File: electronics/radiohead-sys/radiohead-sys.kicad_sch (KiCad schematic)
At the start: 0 parts

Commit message: cleaning up radiohead system overview to blank slate
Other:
- note removed: "Device Table"
- note removed: "Radiohead Robot"
- title: RADIOHEAD -> Radio-Head Robot

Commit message: completing all major schematics, just need to add usb devices
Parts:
- added D1: LED_Small, symbol Device:LED_Small
- added J2: JETSON_NANO.J41, symbol Connector_Generic:Conn_02x20_Odd_Even
- added J3: JETSON_NANO.J50, symbol Connector_Generic:Conn_01x12
- added Q2: Q_PNP, symbol Device:Q_PNP
- added R1: R_Small, symbol Device:R_Small
- added SW1, SW2: SW_Push, symbol Switch:SW_Push
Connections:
- new net: D1.1 (K), R1.1
- new net: D1.2 (A), Q2.C
- new net: J3.11 (Pin_11), SW1.2
- new net: J3.12 (Pin_12), SW1.1
- new net: J3.5 (Pin_5), J3.6 (Pin_6)
- new net: J3.7 (Pin_7), SW2.2
- new net: J3.8 (Pin_8), SW2.1
- new net ARDUINO_COMM.J41.SPI1.CIPO: J2.21 (Pin_21)
- new net ARDUINO_COMM.J41.SPI1.COPI: J2.19 (Pin_19)
- new net ARDUINO_COMM.J41.SPI1.SCK: J2.23 (Pin_23)
- new net GND: R1.2
- new net SPEAKER.J41.I2S4.LRCK: J2.35 (Pin_35)
- new net SPEAKER.J41.I2S4.SCLK: J2.12 (Pin_12)
- new net SPEAKER.J41.I2S4.SDIN: J2.38 (Pin_38)
- new net SPEAKER.J41.I2S4.SDOUT: J2.40 (Pin_40)
- new net STATUS_LED0.J41.GPIO.OUT: J2.3 (Pin_3)
- new net STATUS_LEDX.<J41, ARDUINO_PINOUT>.GPIO.OUT: Q2.B
- new net VDD: Q2.E
- no-connect marks 0 -> 7
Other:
- added sheet arduino (arduino.kicad_sch)
- added sheet audio (audio.kicad_sch)
- note added: "Circuits to Build * Jetson Nano (wip) - Power, reset buttons (done) - Camera (wip) - Screen(done) - Audio (done) - Microphone (wip) - Status lights (LEDs) (done) - Internet (done) * Arduino/Jetson Interface (done) * Arduino (wip) - pot/knob controller (done) - Servo limit switch (done) - Servo Driver (done) - Status Lights (done) * Power System (todo)"
- note added: "Developer Kit Module Interfaces"
- note added: "J41.P24.SPI1.CS0"
- note added: "Jetson Nano Wiring"
- note added: "Microphone Investigation Curretnly, we have the OSEPP Sound Sensor Module, that gives us an analog voltage reading of the current environmental noise. We would need to pass these values back which would be a bit of a pain. Or if we want the jetson nano to analyze them. Note also the OSEPP sound sensor is made for sound ranges 10-55Hz, whereas human noise is in the ~90-155Hz for male. I think the 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"
- note added: "P.5 + P.6, disable auto-on P.7 + P.8, switch for reset P.11 + P.12, switch for power-on"
- note added: "SPI Alt COPI -> MOSI CIPO -> MISO"
- note added: "SPI Resources - https://learn.sparkfun.com/tutorials/serial-peripheral-interface-spi/all Audio Resources - https://www.sparkfun.com/sparkfun-i2s-audio-breakout-max98357a.html Screen Resources - https://www.adafruit.com/product/1680 - https://www.adafruit.com/product/2218 Camera Resources - https://marketplace.nvidia.com/en-us/enterprise/robotics-edge/?category=cameras&page=1&limit=15 - https://de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"
- note added: "Status LEDs schematic for Jetson Nano and Arduino"
- note added: "Sub-Circuits"
- note added: "To Do List"
- note added: "x2"
- title: Radio-Head Robot -> Radiohead Animatronic

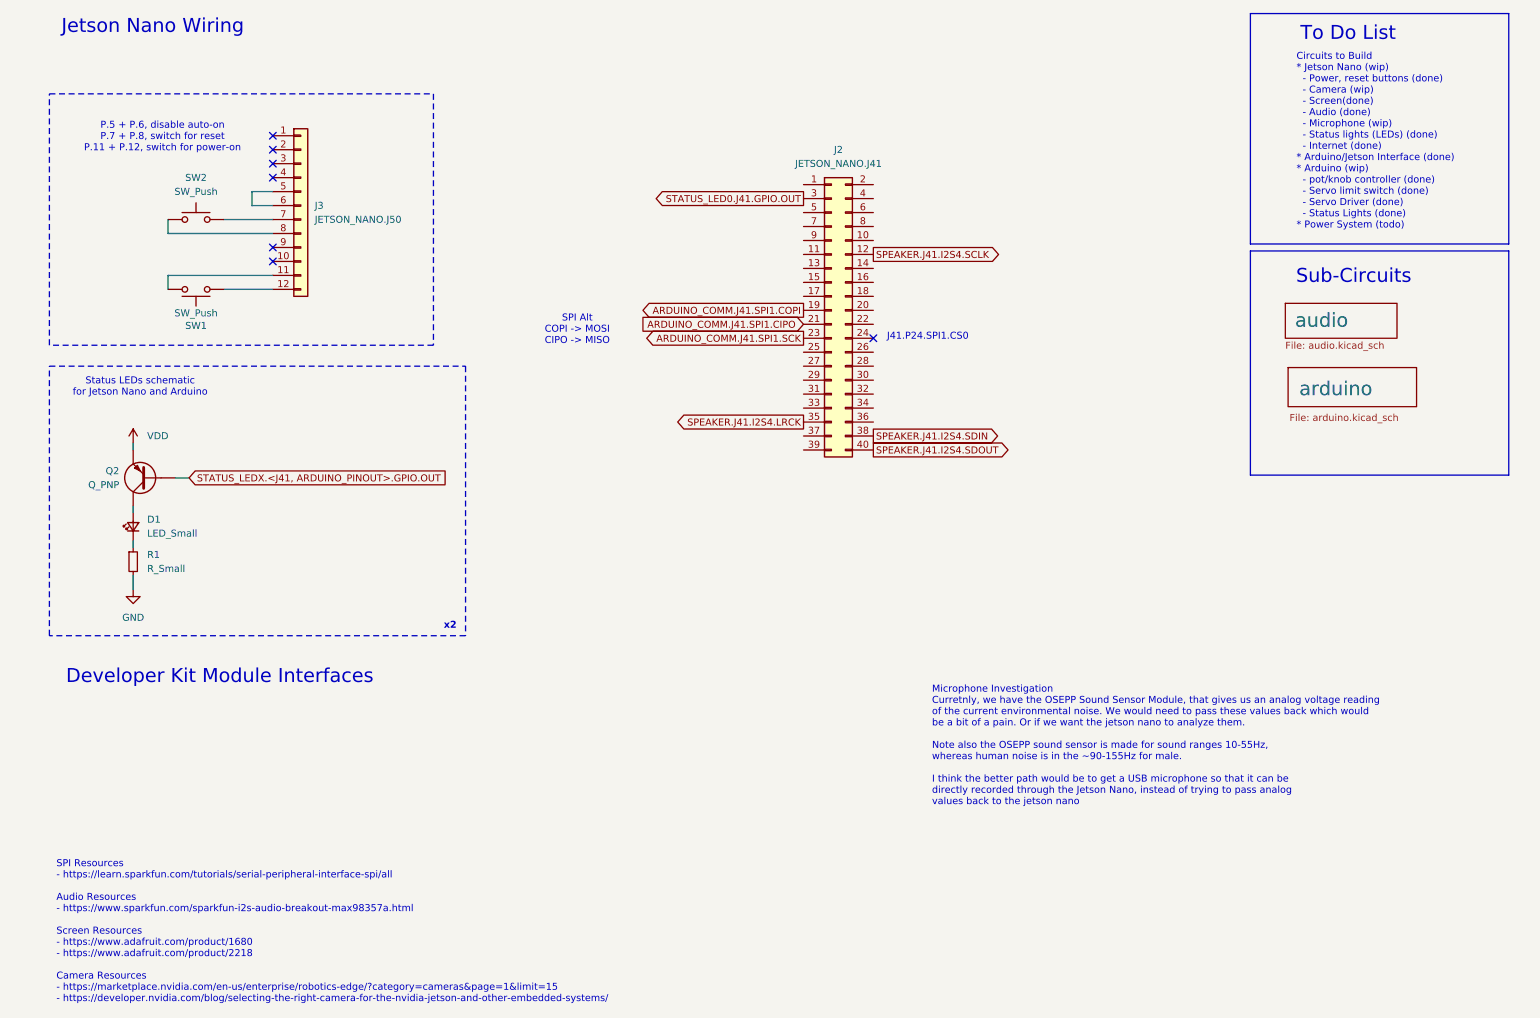
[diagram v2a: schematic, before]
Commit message: added microphone and camera parts
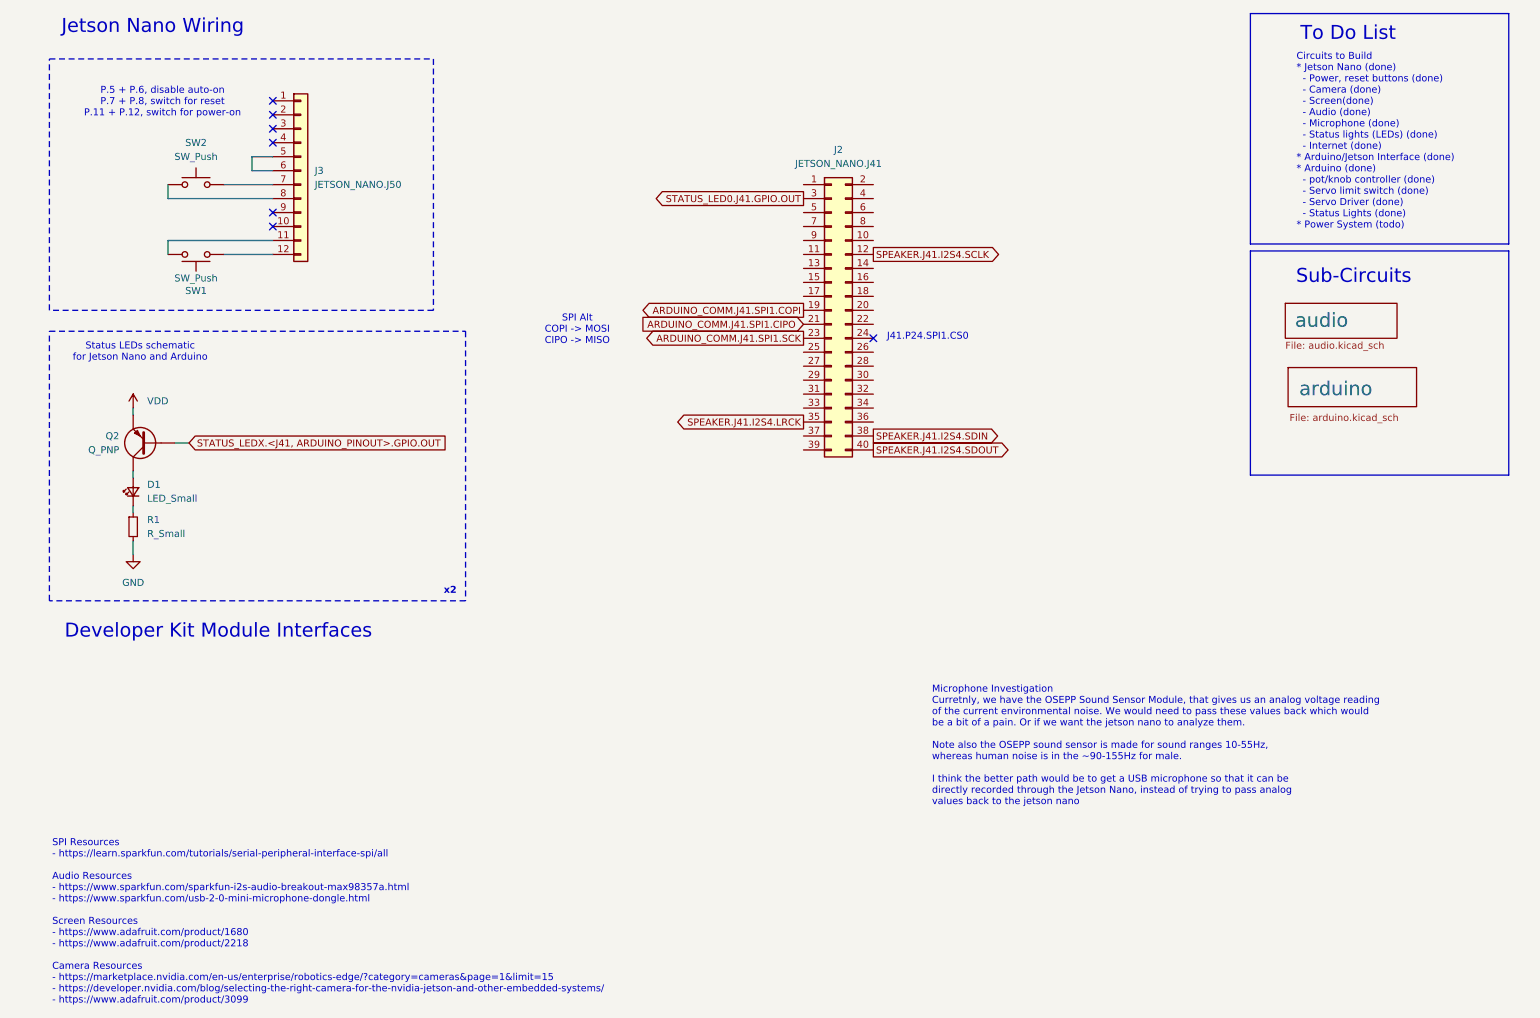
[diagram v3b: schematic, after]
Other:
- note added: "Circuits to Build * Jetson Nano (done) - Power, reset buttons (done) - Camera (done) - Screen(done) - Audio (done) - Microphone (done) - Status lights (LEDs) (done) - Internet (done) * Arduino/Jetson Interface (done) * Arduino (done) - pot/knob controller (done) - Servo limit switch (done) - Servo Driver (done) - Status Lights (done) * Power System (todo)"
- note added: "SPI Resources - https://learn.sparkfun.com/tutorials/serial-peripheral-interface-spi/all Audio Resources - https://www.sparkfun.com/sparkfun-i2s-audio-breakout-max98357a.html - https://www.sparkfun.com/usb-2-0-mini-microphone-dongle.html Screen Resources - https://www.adafruit.com/product/1680 - https://www.adafruit.com/product/2218 Camera Resources - https://marketplace.nvidia.com/en-us/enterpri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"
- note removed: "Circuits to Build * Jetson Nano (wip) - Power, reset buttons (done) - Camera (wip) - Screen(done) - Audio (done) - Microphone (wip) - Status lights (LEDs) (done) - Internet (done) * Arduino/Jetson Interface (done) * Arduino (wip) - pot/knob controller (done) - Servo limit switch (done) - Servo Driver (done) - Status Lights (done) * Power System (todo)"
- note removed: "SPI Resources - https://learn.sparkfun.com/tutorials/serial-peripheral-interface-spi/all Audio Resources - https://www.sparkfun.com/sparkfun-i2s-audio-breakout-max98357a.html Screen Resources - https://www.adafruit.com/product/1680 - https://www.adafruit.com/product/2218 Camera Resources - https://marketplace.nvidia.com/en-us/enterprise/robotics-edge/?category=cameras&page=1&limit=15 - https://de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"
- moved on the sheet: D1, J3, Q2, R1, SW1, SW2
